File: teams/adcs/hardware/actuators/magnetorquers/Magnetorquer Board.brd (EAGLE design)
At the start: 90 x 90 mm, 31 parts

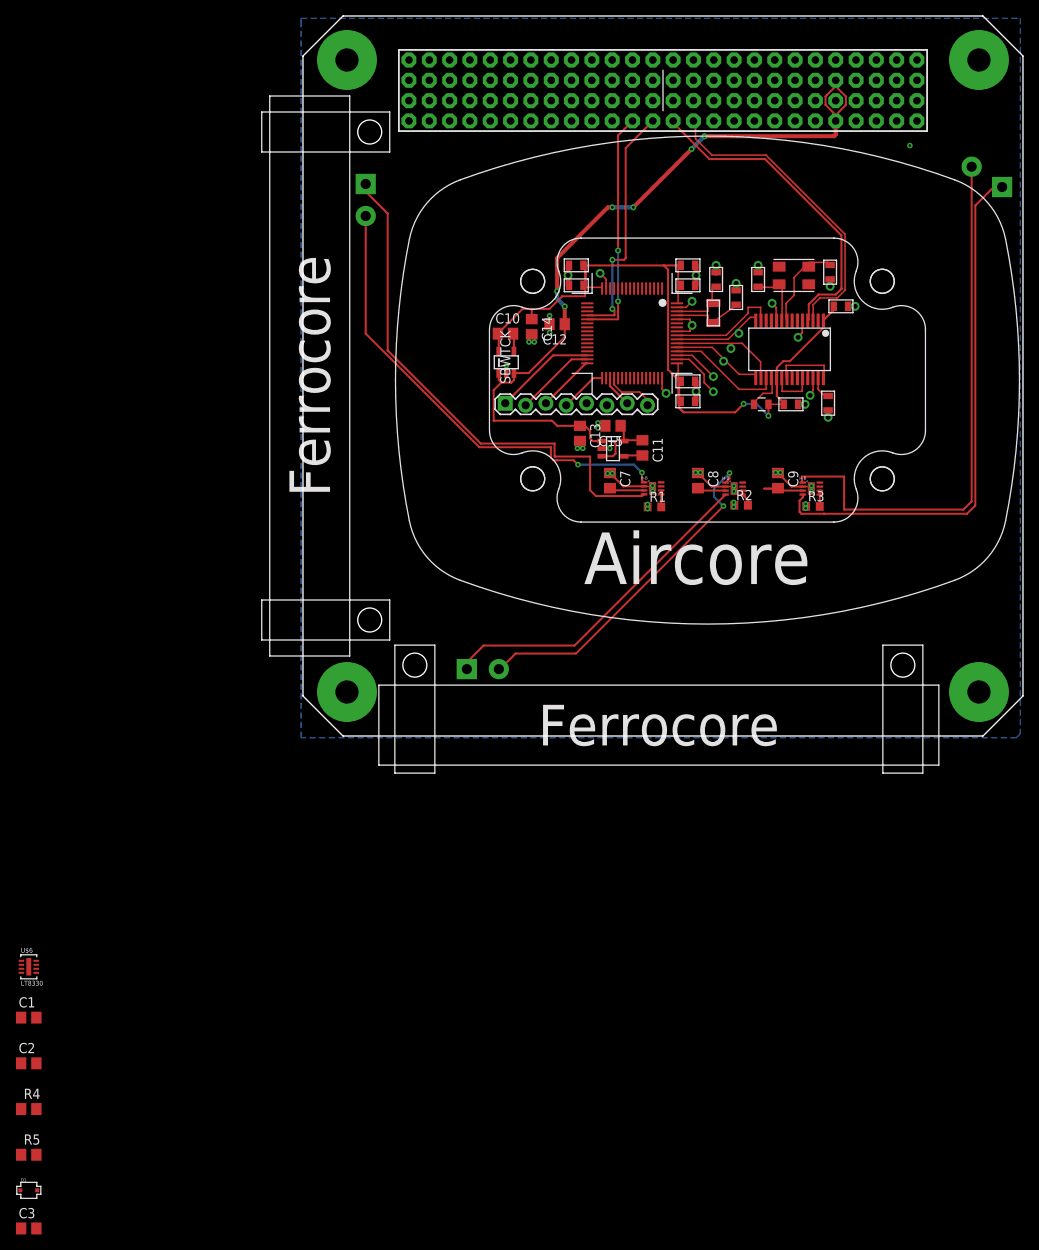
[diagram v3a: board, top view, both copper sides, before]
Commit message: ADCS/MT: Rerouted with new power converter
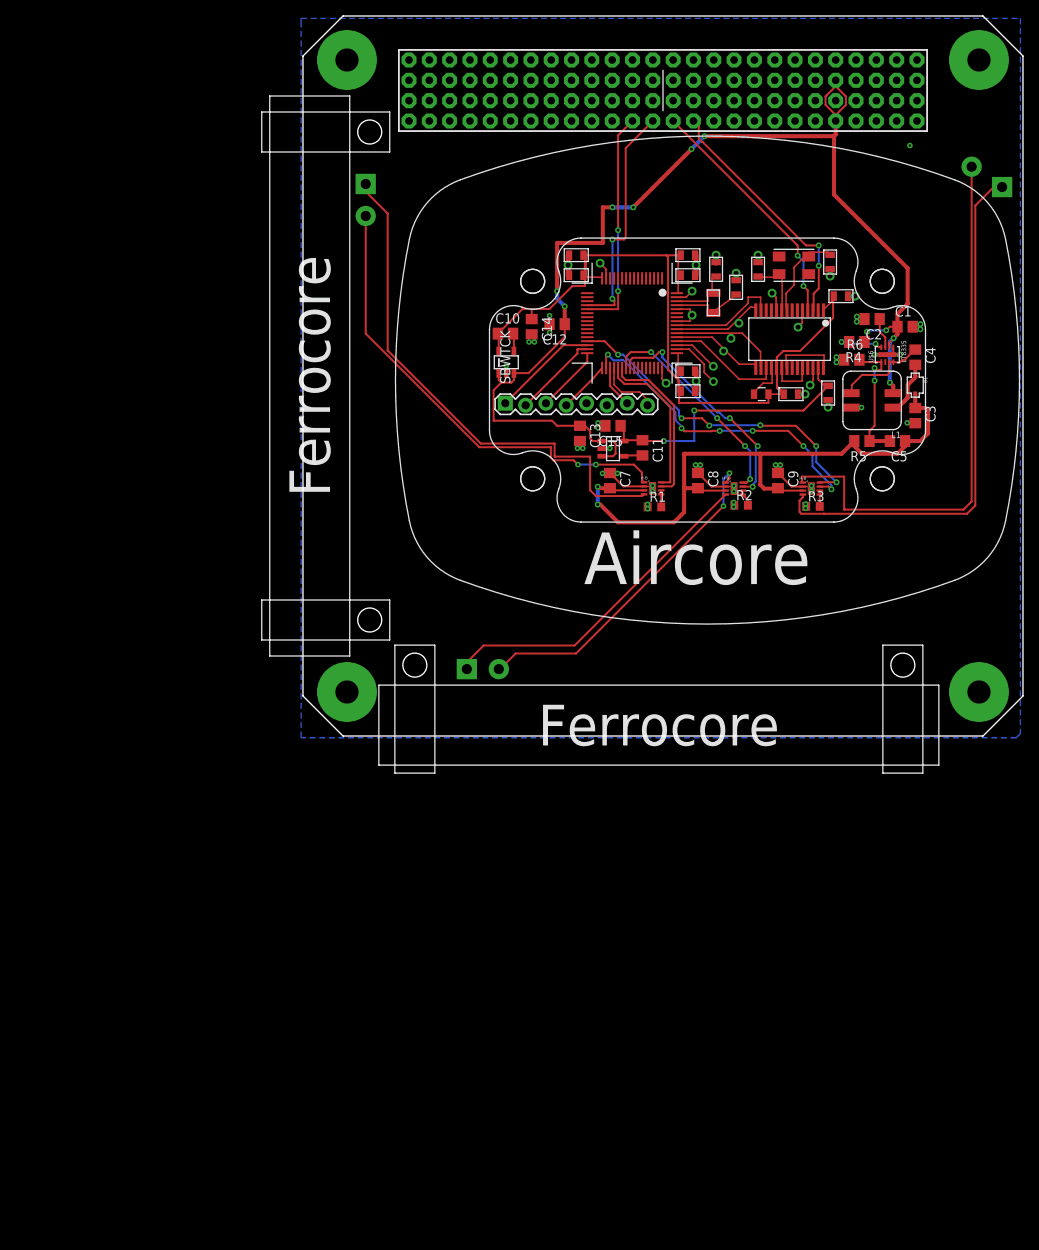
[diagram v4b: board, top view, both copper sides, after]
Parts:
- added C4, C5: (no value), rcl:C0805
- added L1: WURTH_ELEKTRONIK_INDDD_744877001, DubSat1 Components:WURTH_ELEKTRONIK_INDDD_744877001
- added R6: (no value), rcl:R0805
- U$6: value LT8330 -> LT8335
- moved C3 150.3 mm to (87.9, 38.7), turned to 270 degrees
- moved D1 149.7 mm to (87.9, 42.5), turned to 270 degrees
- moved R4 141.1 mm to (80.6, 47.9), turned to 180 degrees
- moved C2 140.6 mm to (82.5, 50.8), turned to 180 degrees
- moved C1 139.5 mm to (86.7, 49.8)
- moved R5 137.1 mm to (81.3, 35.6), turned to 180 degrees
- moved U$6 131.8 mm to (84.5, 46.4), turned to 90 degrees
- moved U$7 1.27 mm to (52.6, 50.3)
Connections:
- net N$4 renamed INT_VCC
- removed net N$3: D1.P$2, U$6.P$3, U$6.P$4
- removed net N$5: R4.2, R5.1, U$6.P$8
- new net EN_UVLO: R4.2, U$6.P$8
- new net FBX: C5.2, R5.1, R6.2, U$6.P$1
- new net N$6: C4.2, D1.P$1, L1.P$1
- new net SW: C4.1, L1.P$3, U$6.P$3, U$6.P$4
- net 6V: now also C5.1, D1.P$2, R5.2; no longer D1.P$1
- net GND: now also L1.P$2, R6.1; no longer R5.2
- net VBAT: now also L1.P$4
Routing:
- net 6V: track 13.0 -> 82.7 mm, vias 0 -> 2
- net VBAT: track 103.2 -> 151.1 mm, vias 6 -> 10
- net PWM_Z_2: track 0.00 -> 42.2 mm, vias 0 -> 6
- net PWM_Z_1: track 0.00 -> 40.2 mm, vias 0 -> 6
- net PWM_X_1: track 0.00 -> 29.5 mm, vias 0 -> 4
- net +5V: track 4.45 -> 33.0 mm, vias 0 -> 2
- net PWM_X_2: track 0.00 -> 26.9 mm, vias 0 -> 4
- net PWM_Y_1: track 0.00 -> 20.6 mm
- net PWM_Y_2: track 0.00 -> 19.8 mm
- net GND: track 23.5 -> 41.4 mm, vias 29 -> 39
- net FBX: track 0.00 -> 16.7 mm, vias 0 -> 2
- net SW: track 0.00 -> 11.7 mm
- net CANH: track 40.8 -> 30.6 mm, vias 0 -> 2
- net CANL: track 39.3 -> 31.4 mm, vias 0 -> 2
- net N$6: track 0.00 -> 6.82 mm
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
